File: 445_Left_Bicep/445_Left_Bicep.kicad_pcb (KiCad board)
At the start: 2 copper layers, 60.1 x 48.6 mm, 5 parts, among them J1 69167-114HLF, J2 SM02B-SRSS-TB_LF__SN_, U1 ESP32-WROOM-32, U2 LSM6DSMTR, U3 LP2950CZ-3.3_LFT3

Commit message: Layout First Draft
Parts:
- added C1: 100nF, CL21F104ZAANNNC:CAPC2012X135N, F.Cu at (150.6, 112.0)
- added C2: 100nF, CL21F104ZAANNNC:CAPC2012X135N, F.Cu at (150.6, 117.1)
- added H1: MountingHole, MountingHole:MountingHole_2mm, F.Cu at (110.1, 66.7)
- added H2: MountingHole, MountingHole:MountingHole_2mm, F.Cu at (153.7, 66.7)
- added H3: MountingHole, MountingHole:MountingHole_2mm, F.Cu at (110.1, 133.0)
- added H4: MountingHole, MountingHole:MountingHole_2mm, F.Cu at (153.7, 133.0)
- added J3: 87583-2010RPLF, 87583-2010RPLF:AMPHENOL_87583-2010RPLF, F.Cu at (121.4, 112.1)
- added J4: 69167-107HLF, 69167-107HLF:AMPHENOL_69167-107HLF, F.Cu at (137.7, 129.7)
- added R1: 10k, RMCF0805JG10K0:RESC2012X65N, F.Cu at (150.6, 122.2)
- added U4: LP2950CZ-3.3_LFT3, LP2950CZ-3.3_LFT3:TO92127P521H735-3, F.Cu at (113.8, 97.3)
- added U5: TS3A5018D, TS3A5018D:SOIC127P600X175-16N, F.Cu at (137.7, 110.8)
- J1: value 69167-114HLF -> 69167-107HLF; footprint 69167-114HLF:AMPHENOL_69167-114HLF -> 69167-107HLF:AMPHENOL_69167-107HLF
- U1: value ESP32-WROOM-32 -> LSM6DSMTR; footprint RF_Module:ESP32-WROOM-32 -> LSM6DSMTR (1):PQFN50P300X250X86-14N
- U2: value LSM6DSMTR -> ESP32-S3-WROOM-1-N16R8; footprint LSM6DSMTR (1):PQFN50P300X250X86-14N -> ESP32-S3-WROOM-1-N16R8:XCVR_ESP32-S3-WROOM-1-N16R8
- U3: value LP2950CZ-3.3_LFT3 -> TS3A5018D; footprint LP2950CZ-3.3_LFT3:TO92127P521H735-3 -> TS3A5018D:SOIC127P600X175-16N
- moved J2 47.4 mm to (113.2, 84.3), turned to -90 degrees
- moved U2 29.3 mm to (136.9, 80.0)
- moved U1 26.4 mm to (150.3, 108.2)
- moved J1 20.6 mm to (137.7, 120.4)
- moved U3 13.1 mm to (137.8, 101.0), turned to 90 degrees
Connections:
- J1 pad 03: unconnected-(J1-Pad03) -> INT1_1
- J1 pad 04: MISO -> MISO_1
- J1 pad 05: MOSI -> MOSI_1
- J1 pad 06: CLK -> CLK1
- J1 pad 07: CS2 -> SENSOR_1
- J2 pad 1: Net-(U3-IN) -> /3.7V
- U1 pad 1: GND -> MISO_2
- U1 pad 12: unconnected-(U1-IO27-Pad12) -> SENSOR_2
- U1 pad 13: unconnected-(U1-IO14-Pad13) -> CLK2
- U1 pad 14: unconnected-(U1-IO12-Pad14) -> MOSI_2
- U1 pad 2: 3.3V -> GND
- U1 pad 3: unconnected-(U1-EN-Pad3) -> GND
- U1 pad 4: unconnected-(U1-SENSOR_VP-Pad4) -> INT1_2
- U1 pad 5: unconnected-(U1-SENSOR_VN-Pad5) -> +3.3V
- U1 pad 6: unconnected-(U1-IO34-Pad6) -> GND
- U1 pad 7: unconnected-(U1-IO35-Pad7) -> GND
- U1 pad 8: unconnected-(U1-IO32-Pad8) -> +3.3V
- U2 pad 1: MISO -> GND
- U2 pad 10: unconnected-(U2-OCS_AUX-Pad10) -> INT1_3
- U2 pad 12: CS1 -> Net-(BZ1-+)
- U2 pad 13: CLK -> D-
- U2 pad 14: MOSI -> D+
- U2 pad 2: GND -> +3.3V
- U2 pad 3: GND -> +3.3V
- U2 pad 6: GND -> unconnected-(U2-IO6-Pad6)
- U2 pad 7: GND -> unconnected-(U2-IO7-Pad7)
- U2 pad 8: +3.3V -> INT1_1
- U2 pad 9: unconnected-(U2-INT2/DEN/MDRDY-Pad9) -> INT1_2
- U3 pad 1: 3.3V -> SENSOR_SEL
- U3 pad 2: GND -> SENSOR_2
- U3 pad 3: Net-(U3-IN) -> SENSOR_1
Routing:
- net +3.3V: track 0.00 -> 123.1 mm
- net INT1_3: track 0.00 -> 51.7 mm, vias 0 -> 1
- net INT1_2: track 0.00 -> 44.8 mm, vias 0 -> 2
- net INT1_1: track 0.00 -> 43.3 mm, vias 0 -> 1
- net SENSOR_3: track 0.00 -> 25.7 mm
- net D+: track 0.00 -> 24.9 mm, vias 0 -> 2
- net D-: track 0.00 -> 24.8 mm, vias 0 -> 2
- net SENSOR_1: track 0.00 -> 23.9 mm, vias 0 -> 2
- net MISO_3: track 0.00 -> 23.0 mm, vias 0 -> 1
- net MOSI_3: track 0.00 -> 22.7 mm, vias 0 -> 1
- net MOSI_1: track 0.00 -> 22.3 mm, vias 0 -> 1
- net MISO_1: track 0.00 -> 22.1 mm, vias 0 -> 1
- net MOSI_2: track 0.00 -> 21.1 mm, vias 0 -> 2
- net CLK3: track 0.00 -> 20.6 mm, vias 0 -> 1
- net MISO_2: track 0.00 -> 20.4 mm, vias 0 -> 2
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- added copper zone on F.Cu, net GND
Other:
- board size 60.1 x 48.6 mm -> 48.6 x 71.4 mm
- board text added: "J2"
- board text added: "Left Bicep Version 1"

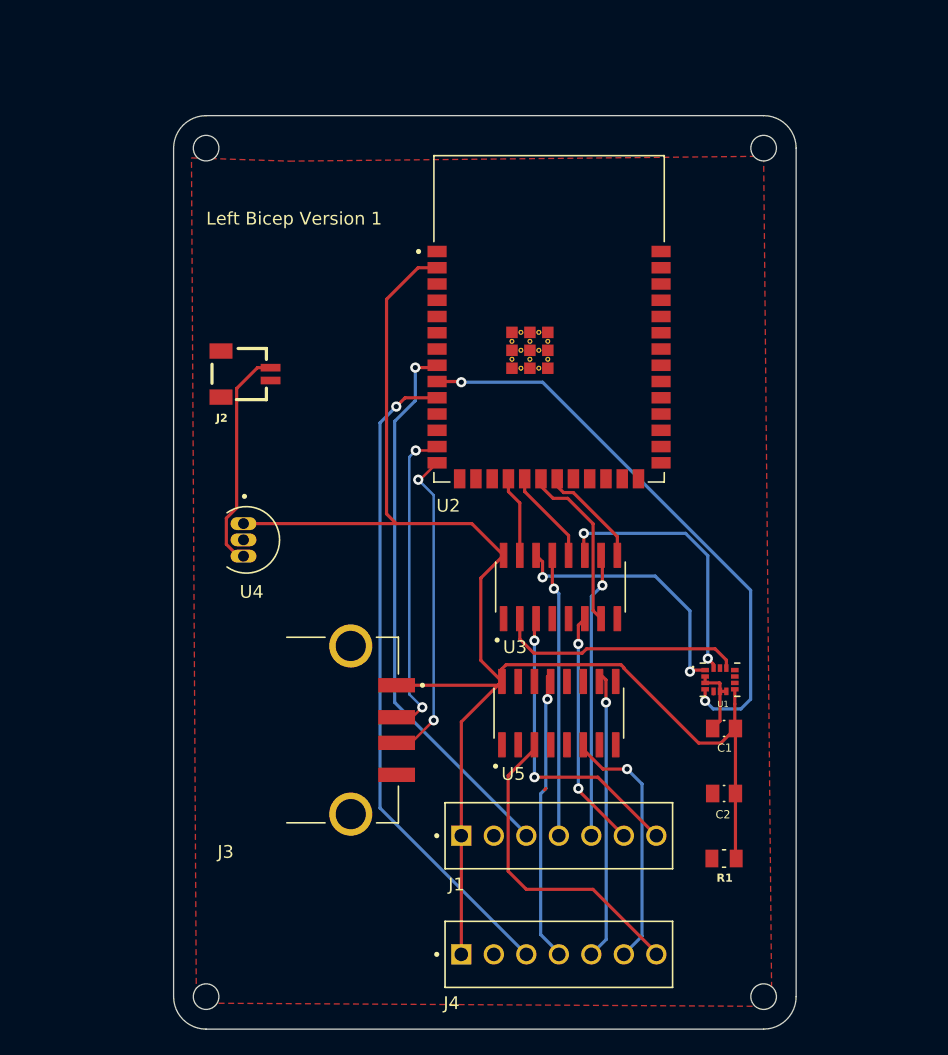
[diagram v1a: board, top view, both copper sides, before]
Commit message: adding buzzer
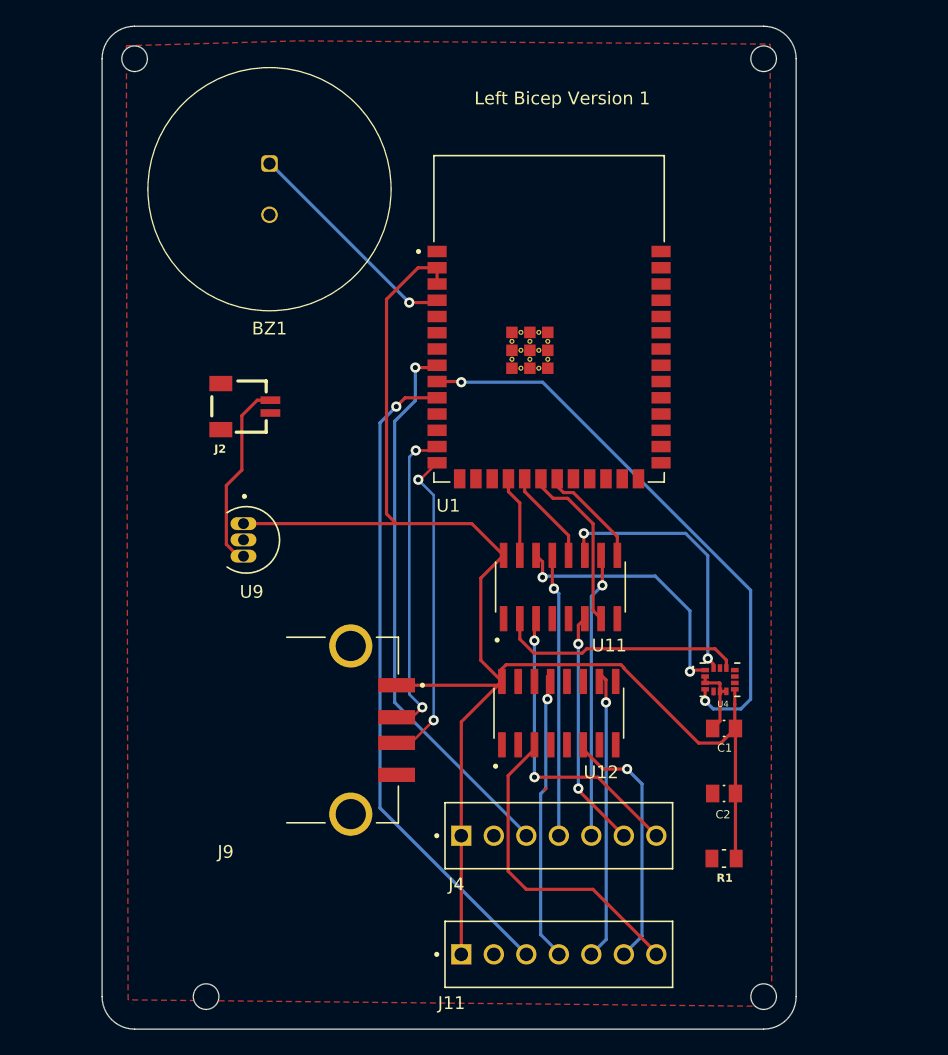
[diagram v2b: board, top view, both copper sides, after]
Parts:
- added BZ1: Buzzer, ECE 445 Footprints:AC-903-D-1P, F.Cu at (115.1, 69.9)
- moved H1 8.95 mm to (104.5, 59.7)
- moved H2 6.98 mm to (153.7, 59.7)
- moved J1 2.54 mm to (113.2, 86.9)
- renumbered J2 to J1, J4 to J11, J1 to J4, J3 to J9, U2 to U1, U3 to U11, U5 to U12, U1 to U4, U4 to U9
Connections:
- U1 pad 12: Net-(BZ1-+) -> unconnected-(U2-IO8-Pad12)
- U1 pad 4: unconnected-(U2-IO4-Pad4) -> Net-(BZ1-+)
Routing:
- net Net-(BZ1-+): track 0.00 -> 17.8 mm, vias 0 -> 1
- net /3.7V: track 17.6 -> 15.0 mm
- net +3.3V: track 123.1 -> 124.3 mm
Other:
- board size 48.6 x 71.4 mm -> 54.2 x 78.4 mm

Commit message: Edits 3/12
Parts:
- moved R1 50.0 mm to (121.0, 81.8), turned to -90 degrees
- moved J9 14.5 mm to (106.9, 111.5)
- moved C2 5.27 mm to (146.8, 113.4), turned to 180 degrees
- moved U4 3.99 mm to (146.4, 109.3)
- moved C1 1.96 mm to (151.4, 110.2), turned to 0 degrees
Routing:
- net CS2: track 0.00 -> 29.8 mm, vias 0 -> 2
- net SENSOR_SEL: track 0.00 -> 28.1 mm, vias 0 -> 3
- net MOSI: track 8.37 -> 22.8 mm, vias 0 -> 2
- net D-: track 24.8 -> 39.0 mm
- net D+: track 24.9 -> 39.2 mm
- net MISO: track 7.40 -> 21.1 mm, vias 0 -> 2
- net +3.3V: track 124.3 -> 137.0 mm, vias 0 -> 2
- net CLK2: track 0.00 -> 12.4 mm
- net CLK: track 13.5 -> 24.0 mm, vias 0 -> 2
- net CS1: track 6.35 -> 12.4 mm
- net INT1_2: track 44.8 -> 50.4 mm
- net CLK1: track 18.6 -> 22.8 mm
- net MOSI_2: track 21.1 -> 18.0 mm
- net MISO_2: track 20.4 -> 18.1 mm
- net SENSOR_2: track 19.3 -> 17.0 mm, vias 0 -> 2
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- added copper zone on B.Cu, net GND

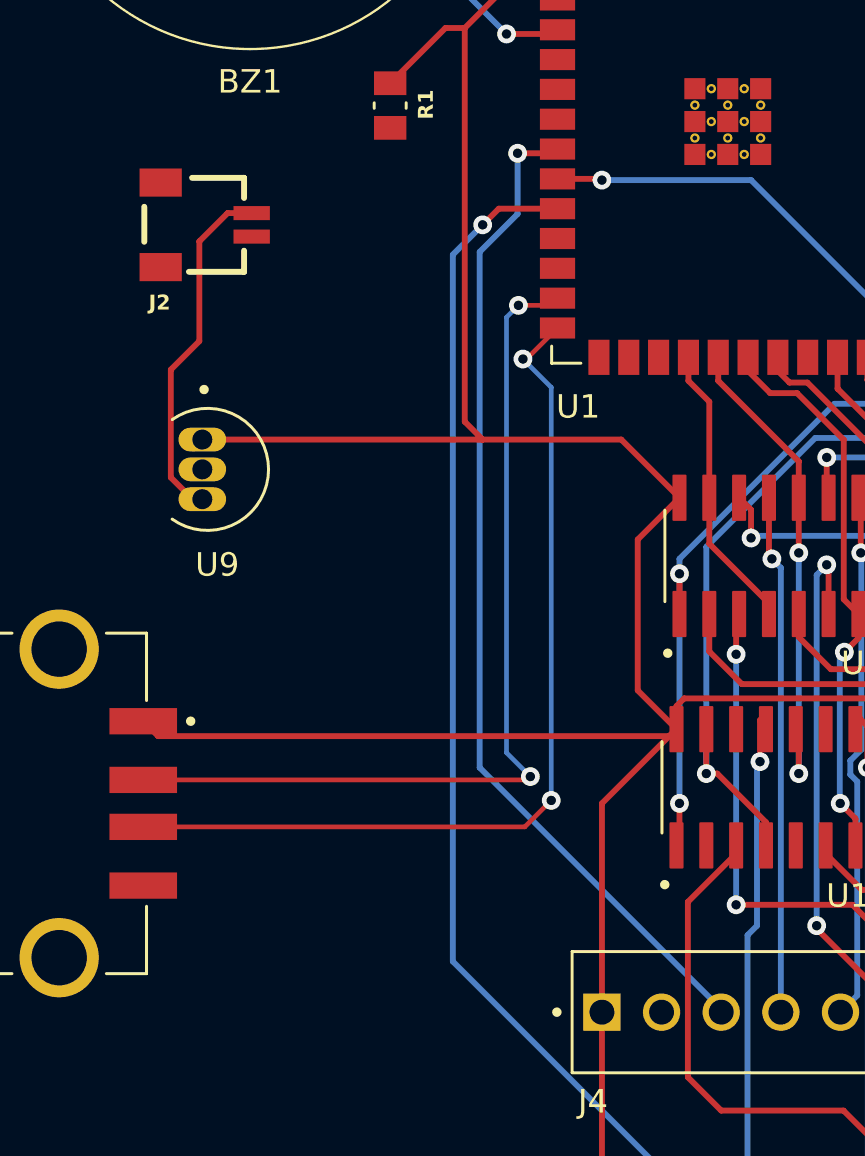
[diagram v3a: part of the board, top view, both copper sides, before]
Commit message: D+ and D- as differential pairs
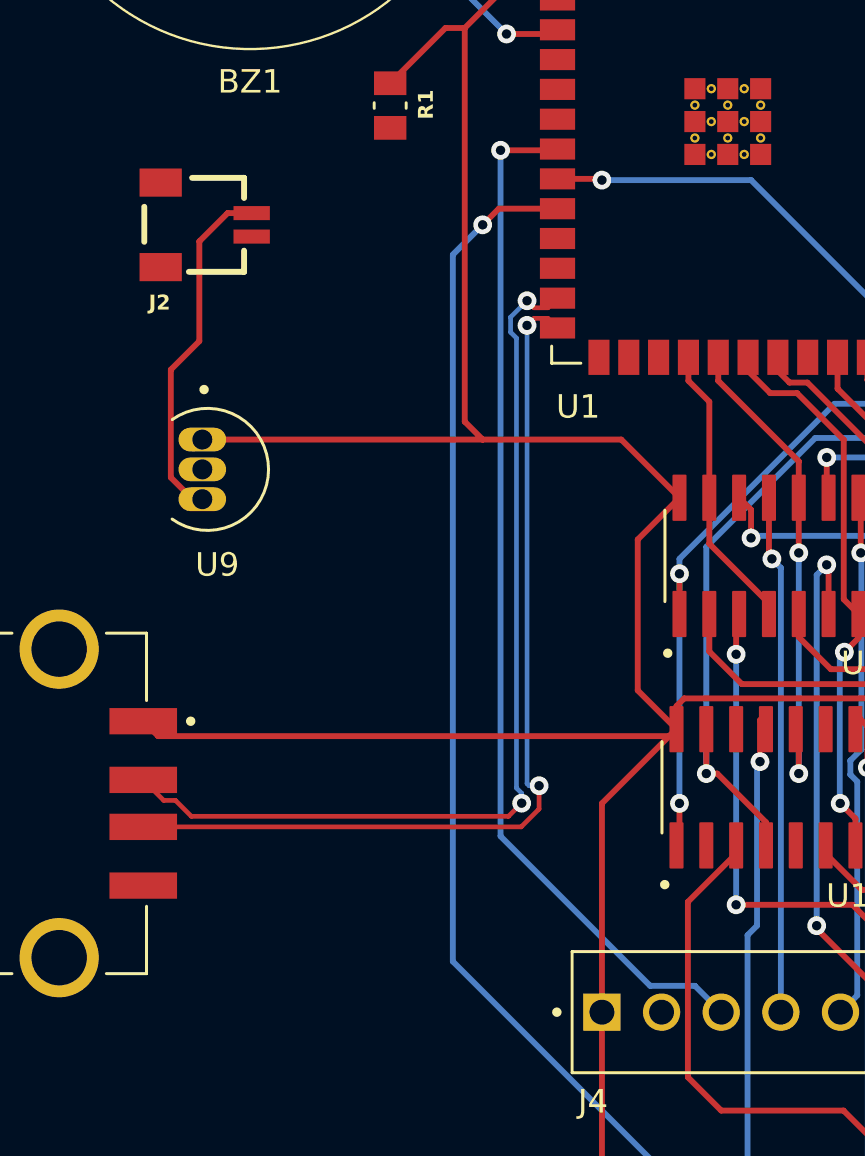
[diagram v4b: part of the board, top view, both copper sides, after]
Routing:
- net D-: track 39.0 -> 40.9 mm
- net INT1_1: track 43.3 -> 44.2 mm
- net D+: track 39.2 -> 39.8 mm
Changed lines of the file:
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@@
   (segment (start 115.062 67.882) (end 115.126 67.882) (width 0.25) (layer "B.Cu") (net 8))
   (segment (start 126.0475 78.8035) (end 125.984 78.74) (width 0.25) (layer "B.Cu") (net 8))
-  (segment (start 127.976 83.82) (end 128.156 83.64) (width 0.25) (layer "F.Cu") (net 9))
-  (segment (start 126.455 83.82) (end 127.976 83.82) (width 0.25) (layer "F.Cu") (net 9))
-  (via (at 126.455 83.82) (size 0.8) (drill 0.4) (layers "F.Cu" "B.Cu") (net 9))
-  (segment (start 126.455 86.406305) (end 126.455 83.82) (width 0.25) (layer "B.Cu") (net 9))
-  (segment (start 124.841 88.020305) (end 126.455 86.406305) (width 0.25) (layer "B.Cu") (net 9))
-  (segment (start 135.128 120.269) (end 124.841 109.982) (width 0.25) (layer "B.Cu") (net 9))
-  (segment (start 124.841 109.982) (end 124.841 88.020305) (width 0.25) (layer "B.Cu") (net 9))
-  (segment (start 135.128 120.396) (end 135.128 120.269) (width 0.25) (layer "B.Cu") (net 9))
+  (segment (start 128.103 83.693) (end 128.156 83.64) (width 0.25) (layer "F.Cu") (net 9))
+  (segment (start 125.73 83.693) (end 128.103 83.693) (width 0.25) (layer "F.Cu") (net 9))
+  (via (at 125.73 83.693) (size 0.8) (drill 0.4) (layers "F.Cu" "B.Cu") (net 9))
+  (segment (start 132.103 119.276) (end 134.008 119.276) (width 0.25) (layer "B.Cu") (net 9))
+  (segment (start 125.73 83.693) (end 125.73 112.903) (width 0.25) (layer "B.Cu") (net 9))
+  (segment (start 125.73 112.903) (end 132.103 119.276) (width 0.25) (layer "B.Cu") (net 9))
+  (segment (start 134.008 119.276) (end 135.128 120.396) (width 0.25) (layer "B.Cu") (net 9))
   (segment (start 137.287 101.092) (end 137.16 100.965) (width 0.25) (layer "F.Cu") (net 10))
   (segment (start 137.16 100.965) (end 137.16 98.49) (width 0.25) (layer "F.Cu") (net 10))
@@
   (via (at 135.763 105.156) (size 0.8) (drill 0.4) (layers "F.Cu" "B.Cu") (net 13))
   (segment (start 135.763 115.824) (end 135.763 105.156) (width 0.25) (layer "B.Cu") (net 13))
-  (segment (start 126.833 92.583) (end 128.156 91.26) (width 0.2) (layer "F.Cu") (net 14))
-  (segment (start 126.684 92.583) (end 126.833 92.583) (width 0.2) (layer "F.Cu") (net 14))
-  (segment (start 110.514 112.506) (end 126.762 112.506) (width 0.2) (layer "F.Cu") (net 14))
-  (segment (start 126.762 112.506) (end 127.889 111.379) (width 0.2) (layer "F.Cu") (net 14))
-  (via (at 126.684 92.583) (size 0.8) (drill 0.4) (layers "F.Cu" "B.Cu") (net 14))
-  (via (at 127.889 111.379) (size 0.8) (drill 0.4) (layers "F.Cu" "B.Cu") (net 14))
-  (segment (start 127.889 93.788) (end 126.684 92.583) (width 0.2) (layer "B.Cu") (net 14))
-  (segment (start 127.889 111.379) (end 127.889 93.788) (width 0.2) (layer "B.Cu") (net 14))
+  (segment (start 127.371232 110.753768) (end 127.371232 111.743718) (width 0.2) (layer "F.Cu") (net 14))
+  (segment (start 127.746001 90.850001) (end 127.157659 90.850001) (width 0.2) (layer "F.Cu") (net 14))
+  (segment (start 128.156 91.26) (end 127.746001 90.850001) (width 0.2) (layer "F.Cu") (net 14))
+  (segment (start 127.157659 90.850001) (end 126.85766 91.15) (width 0.2) (layer "F.Cu") (net 14))
+  (segment (start 127.371232 111.743718) (end 126.60895 112.506) (width 0.2) (layer "F.Cu") (net 14))
+  (segment (start 126.60895 112.506) (end 110.514 112.506) (width 0.2) (layer "F.Cu") (net 14))
+  (via (at 127.371232 110.753768) (size 0.8) (drill 0.4) (layers "F.Cu" "B.Cu") (net 14))
+  (via (at 126.85766 91.15) (size 0.8) (drill 0.4) (layers "F.Cu" "B.Cu") (net 14))
+  (segment (start 126.85766 91.15) (end 126.85766 110.664461) (width 0.2) (layer "B.Cu") (net 14))
+  (segment (start 126.85766 110.664461) (end 126.946967 110.753768) (width 0.2) (layer "B.Cu") (net 14))
+  (segment (start 126.946967 110.753768) (end 127.371232 110.753768) (width 0.2) (layer "B.Cu") (net 14))
+  (segment (start 112.563999 112.055999) (end 111.887 111.379) (width 0.2) (layer "F.Cu") (net 15))
+  (segment (start 127.746001 90.399999) (end 127.157659 90.399999) (width 0.2) (layer "F.Cu") (net 15))
+  (segment (start 127.157659 90.399999) (end 126.85766 90.1) (width 0.2) (layer "F.Cu") (net 15))
   (segment (start 127.849 90.297) (end 128.156 89.99) (width 0.2) (layer "F.Cu") (net 15))
-  (segment (start 110.514 110.506) (end 126.857 110.506) (width 0.2) (layer "F.Cu") (net 15))
-  (segment (start 126.492 90.297) (end 127.849 90.297) (width 0.2) (layer "F.Cu") (net 15))
-  (segment (start 126.857 110.506) (end 127 110.363) (width 0.2) (layer "F.Cu") (net 15))
-  (via (at 126.492 90.297) (size 0.8) (drill 0.4) (layers "F.Cu" "B.Cu") (net 15))
-  (via (at 127 110.363) (size 0.8) (drill 0.4) (layers "F.Cu" "B.Cu") (net 15))
-  (segment (start 125.984 90.805) (end 126.492 90.297) (width 0.2) (layer "B.Cu") (net 15))
-  (segment (start 125.984 109.347) (end 125.984 90.805) (width 0.2) (layer "B.Cu") (net 15))
-  (segment (start 127 110.363) (end 125.984 109.347) (width 0.2) (layer "B.Cu") (net 15))
+  (segment (start 128.156 89.99) (end 127.746001 90.399999) (width 0.2) (layer "F.Cu") (net 15))
+  (segment (start 111.387 111.379) (end 110.514 110.506) (width 0.2) (layer "F.Cu") (net 15))
+  (segment (start 126.628768 111.496232) (end 126.069001 112.055999) (width 0.2) (layer "F.Cu") (net 15))
+  (segment (start 126.069001 112.055999) (end 112.563999 112.055999) (width 0.2) (layer "F.Cu") (net 15))
+  (segment (start 111.887 111.379) (end 111.387 111.379) (width 0.2) (layer "F.Cu") (net 15))
+  (via (at 126.85766 90.1) (size 0.8) (drill 0.4) (layers "F.Cu" "B.Cu") (net 15))
+  (via (at 126.628768 111.496232) (size 0.8) (drill 0.4) (layers "F.Cu" "B.Cu") (net 15))
+  (segment (start 126.628768 111.071967) (end 126.628768 111.496232) (width 0.2) (layer "B.Cu") (net 15))
+  (segment (start 126.15766 90.8) (end 126.15766 91.43995) (width 0.2) (layer "B.Cu") (net 15))
+  (segment (start 126.85766 90.1) (end 126.15766 90.8) (width 0.2) (layer "B.Cu") (net 15))
+  (segment (start 126.40766 110.850859) (end 126.628768 111.071967) (width 0.2) (layer "B.Cu") (net 15))
+  (segment (start 126.40766 91.68995) (end 126.40766 110.850859) (width 0.2) (layer "B.Cu") (net 15))
+  (segment (start 126.15766 91.43995) (end 126.40766 91.68995) (width 0.2) (layer "B.Cu") (net 15))
   (segment (start 125.656 86.18) (end 128.156 86.18) (width 0.25) (layer "F.Cu") (net 16))
   (segment (start 124.968 86.868) (end 125.656 86.18) (width 0.25) (layer "F.Cu") (net 16))
